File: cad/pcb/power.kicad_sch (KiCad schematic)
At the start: 39 parts, among them X1 USB_C_Receptacle_USB2.0, X2 Bat-Conn, X3 NTC-Conn

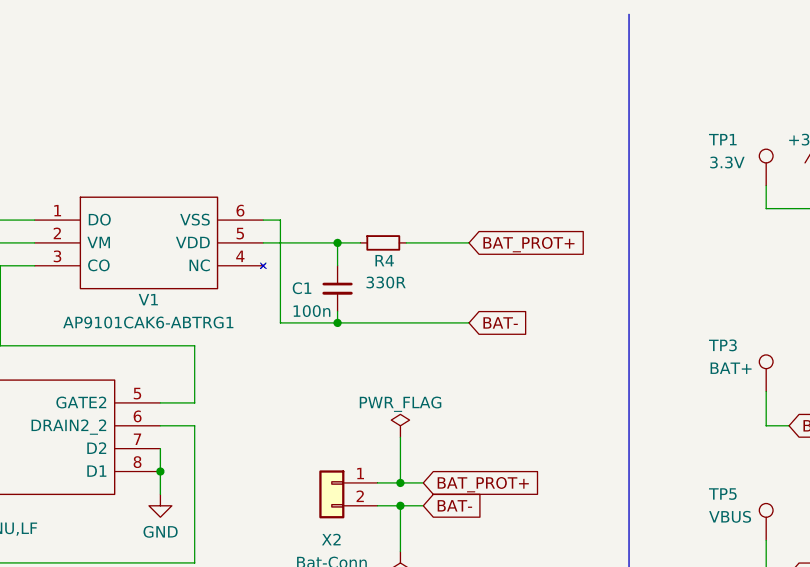
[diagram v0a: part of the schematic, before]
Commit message: generate bom; select C's & L's
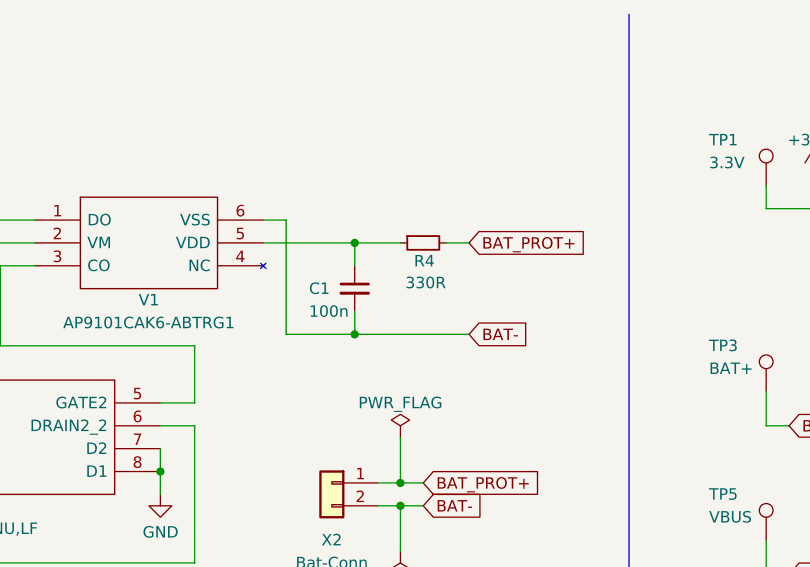
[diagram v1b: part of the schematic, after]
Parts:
- C1, C2, C3, C4, C5, C6, C7: footprint (none) -> Capacitor_SMD:C_0603_1608Metric
- L1, L2: footprint (none) -> Inductor_SMD:L_0603_1608Metric
- R1, R10, R11, R12, R13, R2, R3, R4, R5, R6, R7, R8, R9: footprint (none) -> Resistor_SMD:R_0603_1608Metric
- TP1, TP2, TP3, TP4, TP5, TP8, TP9: footprint (none) -> TestPoint:TestPoint_Pad_D1.0mm
- TP6, TP7: footprint TestPoint:TestPoint_Pad_D2.5mm -> TestPoint:TestPoint_Pad_D1.0mm
- V2: Mouser Part Number (none) -> 757-SSM6N68NULF
- V3: Mouser Part Number (none) -> 576-SP0503BAHTG
- V5: Mouser Part Number (none) -> BQ25606RGET
- X1: footprint myLib:USB_C_Receptacle_Molex_216990-0003 -> myLib:USB_C_Receptacle_Amphenol_12401598; Mouser Part Number (none) -> 12401598E4#2A
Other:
- moved on the sheet: C1, R4
